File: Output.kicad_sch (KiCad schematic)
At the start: 0 parts

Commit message: [WIP] PMUv2
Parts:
- added D17: OUT 1, LED_SMD:LED_0603_1608Metric, symbol Device:LED_Small_Filled
- added D18: Shottky, Diode_SMD:D_SOD-123F, symbol Device:D_Schottky_Small_Filled
- added J24: Output, TXV_Library_Footprints:Molex_Nano-Fit_105309-xx02_1x02_P2.50mm_Vertical, symbol Connector_Generic:Conn_01x02
- added JP7: Jumper_3_Open, Jumper:SolderJumper-3_P1.3mm_Open_RoundedPad1.0x1.5mm, symbol Jumper:Jumper_3_Open
- added Q7: SISA88DN or similar, TXV_Library_Footprints:PowerPAK_1212-8, symbol Device:Q_NMOS_GDS
- added R42, R49: 120, Resistor_SMD:R_0603_1608Metric, symbol Device:R_Small
- added R48: 10k, Resistor_SMD:R_0603_1608Metric, symbol Device:R_Small
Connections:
- new net: D18.1 (K), J24.1 (Pin_1), JP7.2 (C)
- new net: Q7.1 (G), R49.2
- new net: D18.2 (A), J24.2 (Pin_2), Q7.2 (D)
- new net: D17.2 (A), R42.2
- new net +5VP: JP7.3 (B)
- new net Control: R42.1, R48.2, R49.1
- new net GND: D17.1 (K), Q7.3 (S), R48.1
- new net PYRO: JP7.1 (A)

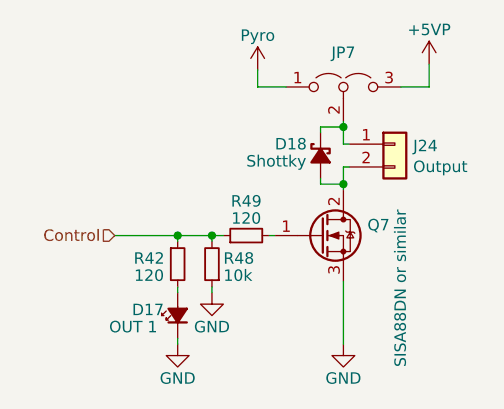
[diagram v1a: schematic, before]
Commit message: V3 Init Commit
Fix of known issues of v2
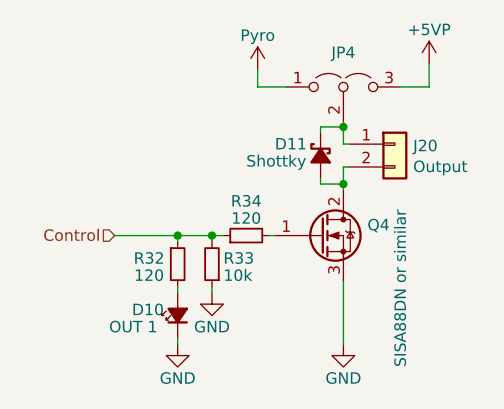
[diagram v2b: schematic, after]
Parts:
- renumbered D17 to D10, D18 to D11, J24 to J20, JP7 to JP4, Q7 to Q4, R42 to R32, R48 to R33, R49 to R34
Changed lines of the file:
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@@
   (symbol (lib_id "power:GND") (at 151.765 90.805 0)
     (in_bom yes) (on_board yes)
-    (property "Reference" "#PWR0107" (id 0) (at 151.765 97.155 0)
+    (property "Reference" "#PWR083" (id 0) (at 151.765 97.155 0)
       (effects (font (size 1.27 1.27)) hide)
     )
@@
   (symbol (lib_id "Jumper:Jumper_3_Open") (at 151.765 62.23 0)
     (in_bom yes) (on_board yes) (fields_autoplaced)
-    (property "Reference" "JP7" (id 0) (at 151.765 58.42 0))
+    (property "Reference" "JP4" (id 0) (at 151.765 58.42 0))
     (property "Value" "Jumper_3_Open" (id 1) (at 151.765 58.42 0)
       (effects (font (size 1.27 1.27)) hide)
@@
   (symbol (lib_id "Device:Q_NMOS_GDS") (at 149.225 78.74 0)
     (in_bom yes) (on_board yes)
-    (property "Reference" "Q7" (id 0) (at 154.432 77.5716 0)
+    (property "Reference" "Q4" (id 0) (at 154.432 77.5716 0)
       (effects (font (size 1.27 1.27)) (justify left))
     )
@@
   (symbol (lib_id "Device:D_Schottky_Small_Filled") (at 149.225 69.85 90) (mirror x)
     (in_bom yes) (on_board yes)
-    (property "Reference" "D18" (id 0) (at 144.145 68.58 90)
+    (property "Reference" "D11" (id 0) (at 144.145 68.58 90)
       (effects (font (size 1.27 1.27)) (justify right))
     )
@@
   (symbol (lib_id "Device:R_Small") (at 133.35 81.915 0)
     (in_bom yes) (on_board yes)
-    (property "Reference" "R42" (id 0) (at 130.175 81.28 0))
+    (property "Reference" "R32" (id 0) (at 130.175 81.28 0))
     (property "Value" "120" (id 1) (at 130.175 83.185 0))
     (property "Footprint" "Resistor_SMD:R_0603_1608Metric" (id 2) (at 133.35 81.915 0)
@@
   (symbol (lib_id "Connector_Generic:Conn_01x02") (at 157.48 68.58 0)
     (in_bom yes) (on_board yes)
-    (property "Reference" "J24" (id 0) (at 159.512 68.7832 0)
+    (property "Reference" "J20" (id 0) (at 159.512 68.7832 0)
       (effects (font (size 1.27 1.27)) (justify left))
     )
@@
   (symbol (lib_id "power:GND") (at 133.35 90.805 0)
     (in_bom yes) (on_board yes)
-    (property "Reference" "#PWR099" (id 0) (at 133.35 97.155 0)
+    (property "Reference" "#PWR080" (id 0) (at 133.35 97.155 0)
       (effects (font (size 1.27 1.27)) hide)
     )
@@
   (symbol (lib_id "Device:R_Small") (at 137.16 81.915 180)
     (in_bom yes) (on_board yes)
-    (property "Reference" "R48" (id 0) (at 138.43 81.28 0)
+    (property "Reference" "R33" (id 0) (at 138.43 81.28 0)
       (effects (font (size 1.27 1.27)) (justify right))
     )
@@
   (symbol (lib_id "power:GND") (at 137.16 85.09 0)
     (in_bom yes) (on_board yes)
-    (property "Reference" "#PWR0100" (id 0) (at 137.16 91.44 0)
+    (property "Reference" "#PWR081" (id 0) (at 137.16 91.44 0)
       (effects (font (size 1.27 1.27)) hide)
     )
@@
   (symbol (lib_id "Device:LED_Small_Filled") (at 133.35 87.63 90)
     (in_bom yes) (on_board yes)
-    (property "Reference" "D17" (id 0) (at 128.27 86.995 90)
+    (property "Reference" "D10" (id 0) (at 128.27 86.995 90)
       (effects (font (size 1.27 1.27)) (justify right))
     )
@@
   (symbol (lib_id "power:+5VP") (at 161.29 59.69 0)
     (in_bom yes) (on_board yes)
-    (property "Reference" "#PWR0108" (id 0) (at 161.29 63.5 0)
+    (property "Reference" "#PWR084" (id 0) (at 161.29 63.5 0)
       (effects (font (size 1.27 1.27)) hide)
     )
@@
   (symbol (lib_id "Device:R_Small") (at 140.97 78.74 90)
     (in_bom yes) (on_board yes)
-    (property "Reference" "R49" (id 0) (at 140.97 74.93 90))
+    (property "Reference" "R34" (id 0) (at 140.97 74.93 90))
     (property "Value" "120" (id 1) (at 140.97 76.835 90))
     (property "Footprint" "Resistor_SMD:R_0603_1608Metric" (id 2) (at 140.97 78.74 0)
@@
   (symbol (lib_id "TXV_Library_Symbols:Pyro") (at 142.24 60.325 0)
     (in_bom yes) (on_board yes)
-    (property "Reference" "#PWR0106" (id 0) (at 142.24 64.135 0)
+    (property "Reference" "#PWR082" (id 0) (at 142.24 64.135 0)
       (effects (font (size 1.27 1.27)) hide)
     )

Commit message: Schematic: Changed Polarity of umbilical connectors Schematic: Added TVS diode to battery_sense Schematic: Some minor prettyfication
Still wrong: Main LiIon Charger Enable connect to STM32
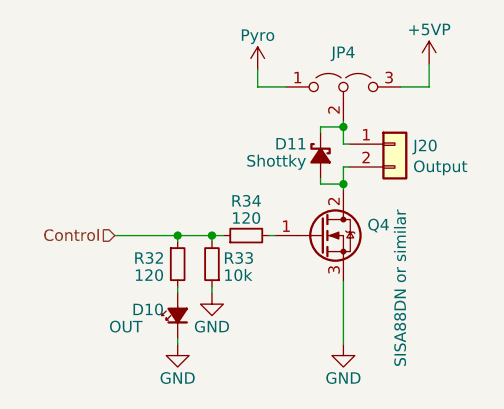
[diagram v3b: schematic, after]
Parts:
- D10: value OUT 1 -> OUT
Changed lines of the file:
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@@
     (effects (font (size 1.27 1.27)) (justify right))
   )
-  (symbol (lib_id "power:GND") (at 151.765 90.805 0)
+  (symbol (lib_id "power:GND") (at 151.765 90.805 0) (unit 1)
     (in_bom yes) (on_board yes)
     (property "Reference" "#PWR083" (id 0) (at 151.765 97.155 0)
@@
     (pin "1")
   )
-  (symbol (lib_id "Jumper:Jumper_3_Open") (at 151.765 62.23 0)
+  (symbol (lib_id "Jumper:Jumper_3_Open") (at 151.765 62.23 0) (unit 1)
     (in_bom yes) (on_board yes) (fields_autoplaced)
     (property "Reference" "JP4" (id 0) (at 151.765 58.42 0))
@@
     (pin "3")
   )
-  (symbol (lib_id "Device:Q_NMOS_GDS") (at 149.225 78.74 0)
+  (symbol (lib_id "Device:Q_NMOS_GDS") (at 149.225 78.74 0) (unit 1)
     (in_bom yes) (on_board yes)
     (property "Reference" "Q4" (id 0) (at 154.432 77.5716 0)
@@
     (pin "3")
   )
-  (symbol (lib_id "Device:D_Schottky_Small_Filled") (at 149.225 69.85 90) (mirror x)
+  (symbol (lib_id "Device:D_Schottky_Small_Filled") (at 149.225 69.85 90) (mirror x) (unit 1)
     (in_bom yes) (on_board yes)
     (property "Reference" "D11" (id 0) (at 144.145 68.58 90)
@@
     (pin "2")
   )
-  (symbol (lib_id "Device:R_Small") (at 133.35 81.915 0)
+  (symbol (lib_id "Device:R_Small") (at 133.35 81.915 0) (unit 1)
     (in_bom yes) (on_board yes)
     (property "Reference" "R32" (id 0) (at 130.175 81.28 0))
@@
     (pin "2")
   )
-  (symbol (lib_id "Connector_Generic:Conn_01x02") (at 157.48 68.58 0)
+  (symbol (lib_id "Connector_Generic:Conn_01x02") (at 157.48 68.58 0) (unit 1)
     (in_bom yes) (on_board yes)
     (property "Reference" "J20" (id 0) (at 159.512 68.7832 0)
@@
     (pin "2")
   )
-  (symbol (lib_id "power:GND") (at 133.35 90.805 0)
+  (symbol (lib_id "power:GND") (at 133.35 90.805 0) (unit 1)
     (in_bom yes) (on_board yes)
     (property "Reference" "#PWR080" (id 0) (at 133.35 97.155 0)
@@
     (pin "1")
   )
-  (symbol (lib_id "Device:R_Small") (at 137.16 81.915 180)
+  (symbol (lib_id "Device:R_Small") (at 137.16 81.915 180) (unit 1)
     (in_bom yes) (on_board yes)
     (property "Reference" "R33" (id 0) (at 138.43 81.28 0)
@@
     (pin "2")
   )
-  (symbol (lib_id "power:GND") (at 137.16 85.09 0)
+  (symbol (lib_id "power:GND") (at 137.16 85.09 0) (unit 1)
     (in_bom yes) (on_board yes)
     (property "Reference" "#PWR081" (id 0) (at 137.16 91.44 0)
@@
     (pin "1")
   )
-  (symbol (lib_id "Device:LED_Small_Filled") (at 133.35 87.63 90)
+  (symbol (lib_id "Device:LED_Small_Filled") (at 133.35 87.63 90) (unit 1)
     (in_bom yes) (on_board yes)
     (property "Reference" "D10" (id 0) (at 128.27 86.995 90)
       (effects (font (size 1.27 1.27)) (justify right))
     )
-    (property "Value" "OUT 1" (id 1) (at 125.73 88.9 90)
+    (property "Value" "OUT" (id 1) (at 125.73 88.9 90)
       (effects (font (size 1.27 1.27)) (justify right))
     )
@@
     (pin "2")
   )
-  (symbol (lib_id "power:+5VP") (at 161.29 59.69 0)
+  (symbol (lib_id "power:+5VP") (at 161.29 59.69 0) (unit 1)
     (in_bom yes) (on_board yes)
     (property "Reference" "#PWR084" (id 0) (at 161.29 63.5 0)
@@
     (pin "1")
   )
-  (symbol (lib_id "Device:R_Small") (at 140.97 78.74 90)
+  (symbol (lib_id "Device:R_Small") (at 140.97 78.74 90) (unit 1)
     (in_bom yes) (on_board yes)
     (property "Reference" "R34" (id 0) (at 140.97 74.93 90))
@@
     (pin "2")
   )
-  (symbol (lib_id "TXV_Library_Symbols:Pyro") (at 142.24 60.325 0)
+  (symbol (lib_id "TXV_Library_Symbols:Pyro") (at 142.24 60.325 0) (unit 1)
     (in_bom yes) (on_board yes)
     (property "Reference" "#PWR082" (id 0) (at 142.24 64.135 0)
